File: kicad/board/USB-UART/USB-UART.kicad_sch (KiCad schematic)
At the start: 17 parts, among them J1 Conn_01x05, J2 Conn_01x02, J3 USB_B_Micro, Q1 MMBF170, U1 MCP2221AxSL

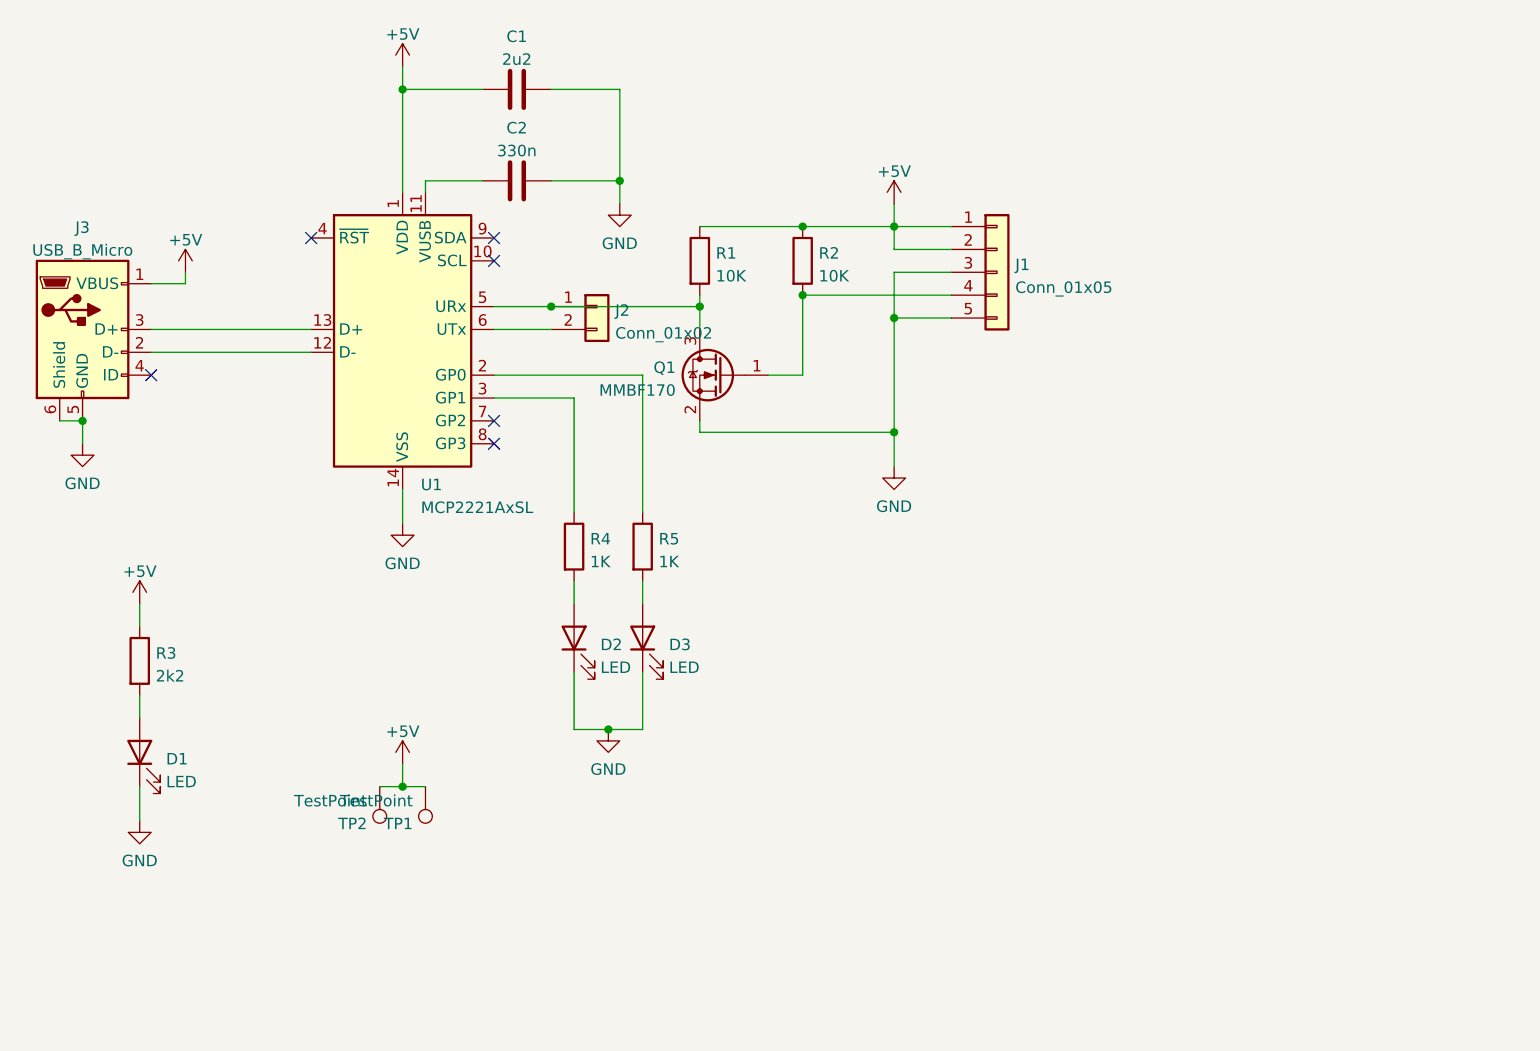
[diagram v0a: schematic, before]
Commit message: hardware: korrekturen fehlerhaftes pcb
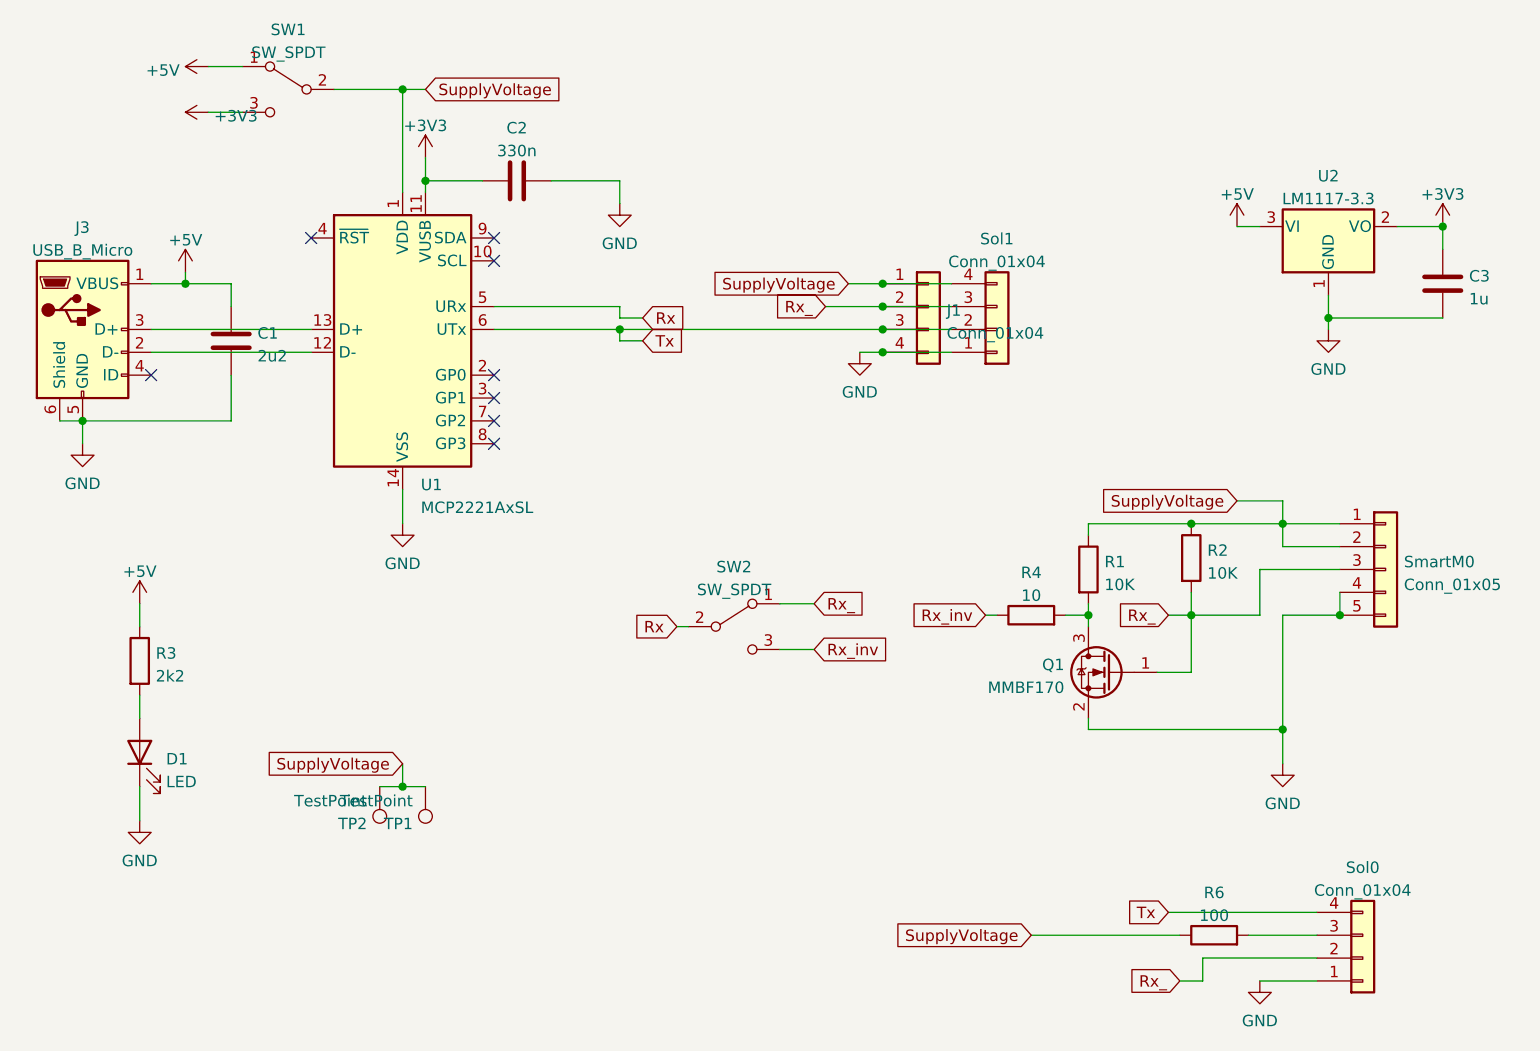
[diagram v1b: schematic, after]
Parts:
- removed D2, D3: LED, LED_SMD:LED_1206_3216Metric, symbol Device:LED
- removed J2: Conn_01x02, Connector_Molex:Molex_KK-254_AE-6410-02A_1x02_P2.54mm_Vertical, symbol Connector_Generic:Conn_01x02
- removed R5: 1K, Resistor_SMD:R_1206_3216Metric, symbol Device:R
- added C3: 1u, Capacitor_SMD:C_1206_3216Metric, symbol Device:C
- added J1: Conn_01x04, Connector_Molex:Molex_KK-254_AE-6410-04A_1x04_P2.54mm_Vertical, symbol Connector_Generic:Conn_01x04
- added R6: 100, Resistor_SMD:R_1206_3216Metric, symbol Device:R
- added SW1, SW2: SW_SPDT, Button_Switch_THT:SW_Slide_1P2T_CK_OS102011MS2Q, symbol Switch:SW_SPDT
- added Sol0, Sol1: Conn_01x04, Connector_JST:JST_PH_B4B-PH-K_1x04_P2.00mm_Vertical, symbol Connector_Generic:Conn_01x04
- added U2: LM1117-3.3, Package_TO_SOT_SMD:SOT-223-3_TabPin2, symbol Regulator_Linear:LM1117-3.3
- R4: value 1K -> 10
- renumbered J1 to SmartM0
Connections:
- net +5V: now also C1.2, SW1.1 (A), U2.3 (VI); no longer C1.1, R1.1, R2.1, SmartM0.1 (Pin_1), SmartM0.2 (Pin_2), TP1.1, TP2.1, U1.1 (VDD)
- net GND: now also C1.1, SmartM0.4 (Pin_4), C3.1, J1.4 (Pin_4), Sol0.1 (Pin_1), Sol1.1 (Pin_1), U2.1 (GND); no longer C1.2, SmartM0.3 (Pin_3)
- net at U1.3 (GP1): no longer R4.1
- net at R4.2: now also Q1.3 (D), R1.2
- net +3V3: now reaches C2.1, U1.11 (VUSB)
- net +3V3: now also C3.2, SW1.3 (C), U2.2 (VO)
- net Tx: now reaches U1.6 (UTx)
- net Tx: now also J1.3 (Pin_3), Sol0.4 (Pin_4), Sol1.2 (Pin_2)
- net Rx_: now reaches Q1.1 (G), R2.2
- net Rx_: now also SmartM0.3 (Pin_3), J1.2 (Pin_2), SW2.1 (A), Sol0.2 (Pin_2), Sol1.3 (Pin_3); no longer SmartM0.4 (Pin_4)
- new net: R6.2, Sol0.3 (Pin_3)
- new net Rx: SW2.2 (B), U1.5 (URx)
- new net Rx_inv: R4.1, SW2.3 (C)
- new net SupplyVoltage: J1.1 (Pin_1), R1.1, R2.1, R6.1, SW1.2 (B), SmartM0.1 (Pin_1), SmartM0.2 (Pin_2), Sol1.4 (Pin_4), TP1.1, TP2.1, U1.1 (VDD)
- no-connect marks 6 -> 8
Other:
- moved on the sheet: C1, Q1, R1, R2, SmartM0
